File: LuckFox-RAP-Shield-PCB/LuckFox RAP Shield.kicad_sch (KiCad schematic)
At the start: 4 parts, among them J1 LuckFox_Pico_Mini_Connector, J2 External_5V_Input_from_Buck_M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, U2 W5500_Ethernet_Module_DNP_on_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

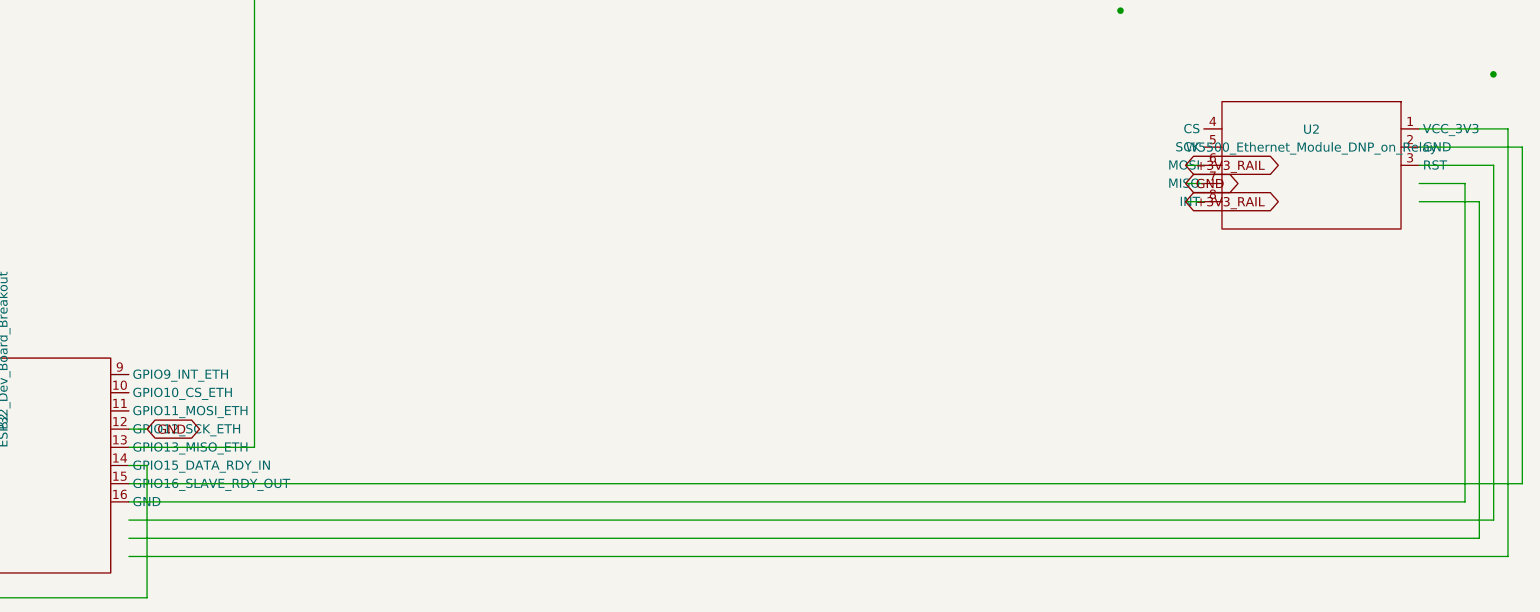
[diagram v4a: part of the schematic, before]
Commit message: Fix U2 wiring: account for its (mirror y) placement flag
U2's instance has a mirror-y flag (set from before this session) that
I missed when computing its pin positions -- both when generating the
SPI-ETH wires/power-rail labels and when validating them, so the
validation was checking its own wrong assumption and passed anyway.
Net effect: CS/SCK/MOSI/MISO/INT are actually on U2's west side and
VCC_3V3/GND/RST on the east, the opposite of what was wired, which is
exactly what was visible in KiCad as wires landing away from the pins.

Recomputed U2's true pin positions with the mirror transform applied
and rerouted the 5 SPI-ETH wires and 3 power-rail label stubs to
match. Re-verified with a corrected, mirror-aware version of the
netlist tracer (all 14 nets correct, zero stray/unconnected pins).
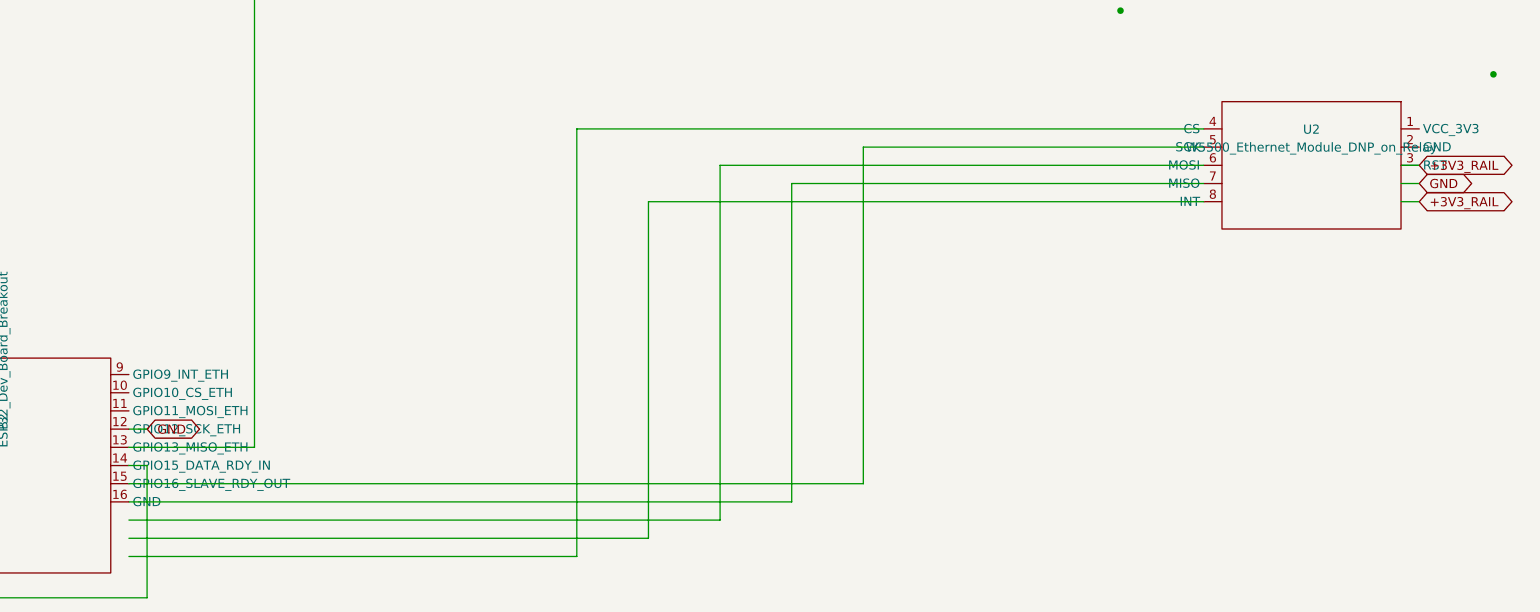
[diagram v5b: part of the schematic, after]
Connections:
- net +3V3_RAIL: now also U2.3 (RST)
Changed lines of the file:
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@@
 	(wire
 		(pts
-			(xy 77.47 189.23) (xy 270 189.23)
-		)
-		(stroke
-			(width 0)
-			(type default)
-		)
-	)
-	(wire
-		(pts
-			(xy 270 189.23) (xy 270 129.54)
-		)
-		(stroke
-			(width 0)
-			(type default)
-		)
-	)
-	(wire
-		(pts
-			(xy 270 129.54) (xy 257.61 129.54)
-		)
-		(stroke
-			(width 0)
-			(type default)
-		)
-	)
-	(wire
-		(pts
-			(xy 77.47 186.69) (xy 266 186.69)
-		)
-		(stroke
-			(width 0)
-			(type default)
-		)
-	)
-	(wire
-		(pts
-			(xy 266 186.69) (xy 266 139.7)
-		)
-		(stroke
-			(width 0)
-			(type default)
-		)
-	)
-	(wire
-		(pts
-			(xy 266 139.7) (xy 257.61 139.7)
-		)
-		(stroke
-			(width 0)
-			(type default)
-		)
-	)
-	(wire
-		(pts
-			(xy 77.47 184.15) (xy 268 184.15)
-		)
-		(stroke
-			(width 0)
-			(type default)
-		)
-	)
-	(wire
-		(pts
-			(xy 268 184.15) (xy 268 134.62)
-		)
-		(stroke
-			(width 0)
-			(type default)
-		)
-	)
-	(wire
-		(pts
-			(xy 268 134.62) (xy 257.61 134.62)
-		)
-		(stroke
-			(width 0)
-			(type default)
-		)
-	)
-	(wire
-		(pts
-			(xy 77.47 181.61) (xy 264 181.61)
-		)
-		(stroke
-			(width 0)
-			(type default)
-		)
-	)
-	(wire
-		(pts
-			(xy 264 181.61) (xy 264 137.16)
-		)
-		(stroke
-			(width 0)
-			(type default)
-		)
-	)
-	(wire
-		(pts
-			(xy 264 137.16) (xy 257.61 137.16)
-		)
-		(stroke
-			(width 0)
-			(type default)
-		)
-	)
-	(wire
-		(pts
-			(xy 77.47 179.07) (xy 272 179.07)
-		)
-		(stroke
-			(width 0)
-			(type default)
-		)
-	)
-	(wire
-		(pts
-			(xy 272 179.07) (xy 272 132.08)
-		)
-		(stroke
-			(width 0)
-			(type default)
-		)
-	)
-	(wire
-		(pts
-			(xy 272 132.08) (xy 257.61 132.08)
+			(xy 77.47 189.23) (xy 140 189.23)
+		)
+		(stroke
+			(width 0)
+			(type default)
+		)
+	)
+	(wire
+		(pts
+			(xy 140 189.23) (xy 140 129.54)
+		)
+		(stroke
+			(width 0)
+			(type default)
+		)
+	)
+	(wire
+		(pts
+			(xy 140 129.54) (xy 227.53 129.54)
+		)
+		(stroke
+			(width 0)
+			(type default)
+		)
+	)
+	(wire
+		(pts
+			(xy 77.47 186.69) (xy 150 186.69)
+		)
+		(stroke
+			(width 0)
+			(type default)
+		)
+	)
+	(wire
+		(pts
+			(xy 150 186.69) (xy 150 139.7)
+		)
+		(stroke
+			(width 0)
+			(type default)
+		)
+	)
+	(wire
+		(pts
+			(xy 150 139.7) (xy 227.53 139.7)
+		)
+		(stroke
+			(width 0)
+			(type default)
+		)
+	)
+	(wire
+		(pts
+			(xy 77.47 184.15) (xy 160 184.15)
+		)
+		(stroke
+			(width 0)
+			(type default)
+		)
+	)
+	(wire
+		(pts
+			(xy 160 184.15) (xy 160 134.62)
+		)
+		(stroke
+			(width 0)
+			(type default)
+		)
+	)
+	(wire
+		(pts
+			(xy 160 134.62) (xy 227.53 134.62)
+		)
+		(stroke
+			(width 0)
+			(type default)
+		)
+	)
+	(wire
+		(pts
+			(xy 77.47 181.61) (xy 170 181.61)
+		)
+		(stroke
+			(width 0)
+			(type default)
+		)
+	)
+	(wire
+		(pts
+			(xy 170 181.61) (xy 170 137.16)
+		)
+		(stroke
+			(width 0)
+			(type default)
+		)
+	)
+	(wire
+		(pts
+			(xy 170 137.16) (xy 227.53 137.16)
+		)
+		(stroke
+			(width 0)
+			(type default)
+		)
+	)
+	(wire
+		(pts
+			(xy 77.47 179.07) (xy 180 179.07)
+		)
+		(stroke
+			(width 0)
+			(type default)
+		)
+	)
+	(wire
+		(pts
+			(xy 180 179.07) (xy 180 132.08)
+		)
+		(stroke
+			(width 0)
+			(type default)
+		)
+	)
+	(wire
+		(pts
+			(xy 180 132.08) (xy 227.53 132.08)
 		)
 		(stroke
@@
 	(wire
 		(pts
-			(xy 227.53 137.16) (xy 224.99 137.16)
-		)
-		(stroke
-			(width 0)
-			(type default)
-		)
-	)
-	(global_label "GND"
-		(shape bidirectional)
-		(at 224.99 137.16 0)
-		(effects
-			(font
-				(size 1.27 1.27)
-			)
-			(justify left)
-		)
-		(property "Intersheetrefs" "${INTERSHEET_REFS}"
-			(at 224.99 137.16 0)
+			(xy 255.07 137.16) (xy 257.61 137.16)
+		)
+		(stroke
+			(width 0)
+			(type default)
+		)
+	)
+	(global_label "GND"
+		(shape bidirectional)
+		(at 257.61 137.16 0)
+		(effects
+			(font
+				(size 1.27 1.27)
+			)
+			(justify left)
+		)
+		(property "Intersheetrefs" "${INTERSHEET_REFS}"
+			(at 257.61 137.16 0)
+			(hide yes)
+			(show_name no)
+			(do_not_autoplace no)
+			(effects
+				(font
+					(size 1.27 1.27)
+				)
+			)
+		)
+	)
+	(wire
+		(pts
+			(xy 255.07 139.7) (xy 257.61 139.7)
+		)
+		(stroke
+			(width 0)
+			(type default)
+		)
+	)
+	(global_label "+3V3_RAIL"
+		(shape bidirectional)
+		(at 257.61 139.7 0)
+		(effects
+			(font
+				(size 1.27 1.27)
+			)
+			(justify left)
+		)
+		(property "Intersheetrefs" "${INTERSHEET_REFS}"
+			(at 257.61 139.7 0)
+			(hide yes)
+			(show_name no)
+			(do_not_autoplace no)
+			(effects
+				(font
+					(size 1.27 1.27)
+				)
+			)
+		)
+	)
+	(wire
+		(pts
+			(xy 255.07 134.62) (xy 257.61 134.62)
+		)
+		(stroke
+			(width 0)
+			(type default)
+		)
+	)
+	(global_label "+3V3_RAIL"
+		(shape bidirectional)
+		(at 257.61 134.62 0)
+		(effects
+			(font
+				(size 1.27 1.27)
+			)
+			(justify left)
+		)
+		(property "Intersheetrefs" "${INTERSHEET_REFS}"
+			(at 257.61 134.62 0)
 			(hide yes)
 			(show_name no)
@@
 			(hide yes)
 			(show_name no)
-			(do_not_autoplace no)
-			(effects
-				(font
-					(size 1.27 1.27)
-				)
-			)
-		)
-	)
-	(wire
-		(pts
-			(xy 227.53 139.7) (xy 224.99 139.7)
-		)
-		(stroke
-			(width 0)
-			(type default)
-		)
-	)
-	(global_label "+3V3_RAIL"
-		(shape bidirectional)
-		(at 224.99 139.7 0)
-		(effects
-			(font
-				(size 1.27 1.27)
-			)
-			(justify left)
-		)
-		(property "Intersheetrefs" "${INTERSHEET_REFS}"
-			(at 224.99 139.7 0)
-			(hide yes)
-			(show_name no)
-			(do_not_autoplace no)
-			(effects
-				(font
-					(size 1.27 1.27)
-				)
-			)
-		)
-	)
-	(wire
-		(pts
-			(xy 227.53 134.62) (xy 224.99 134.62)
-		)
-		(stroke
-			(width 0)
-			(type default)
-		)
-	)
-	(global_label "+3V3_RAIL"
-		(shape bidirectional)
-		(at 224.99 134.62 0)
-		(effects
-			(font
-				(size 1.27 1.27)
-			)
-			(justify left)
-		)
-		(property "Intersheetrefs" "${INTERSHEET_REFS}"
-			(at 224.99 134.62 0)
-			(hide yes)
-			(show_name no)

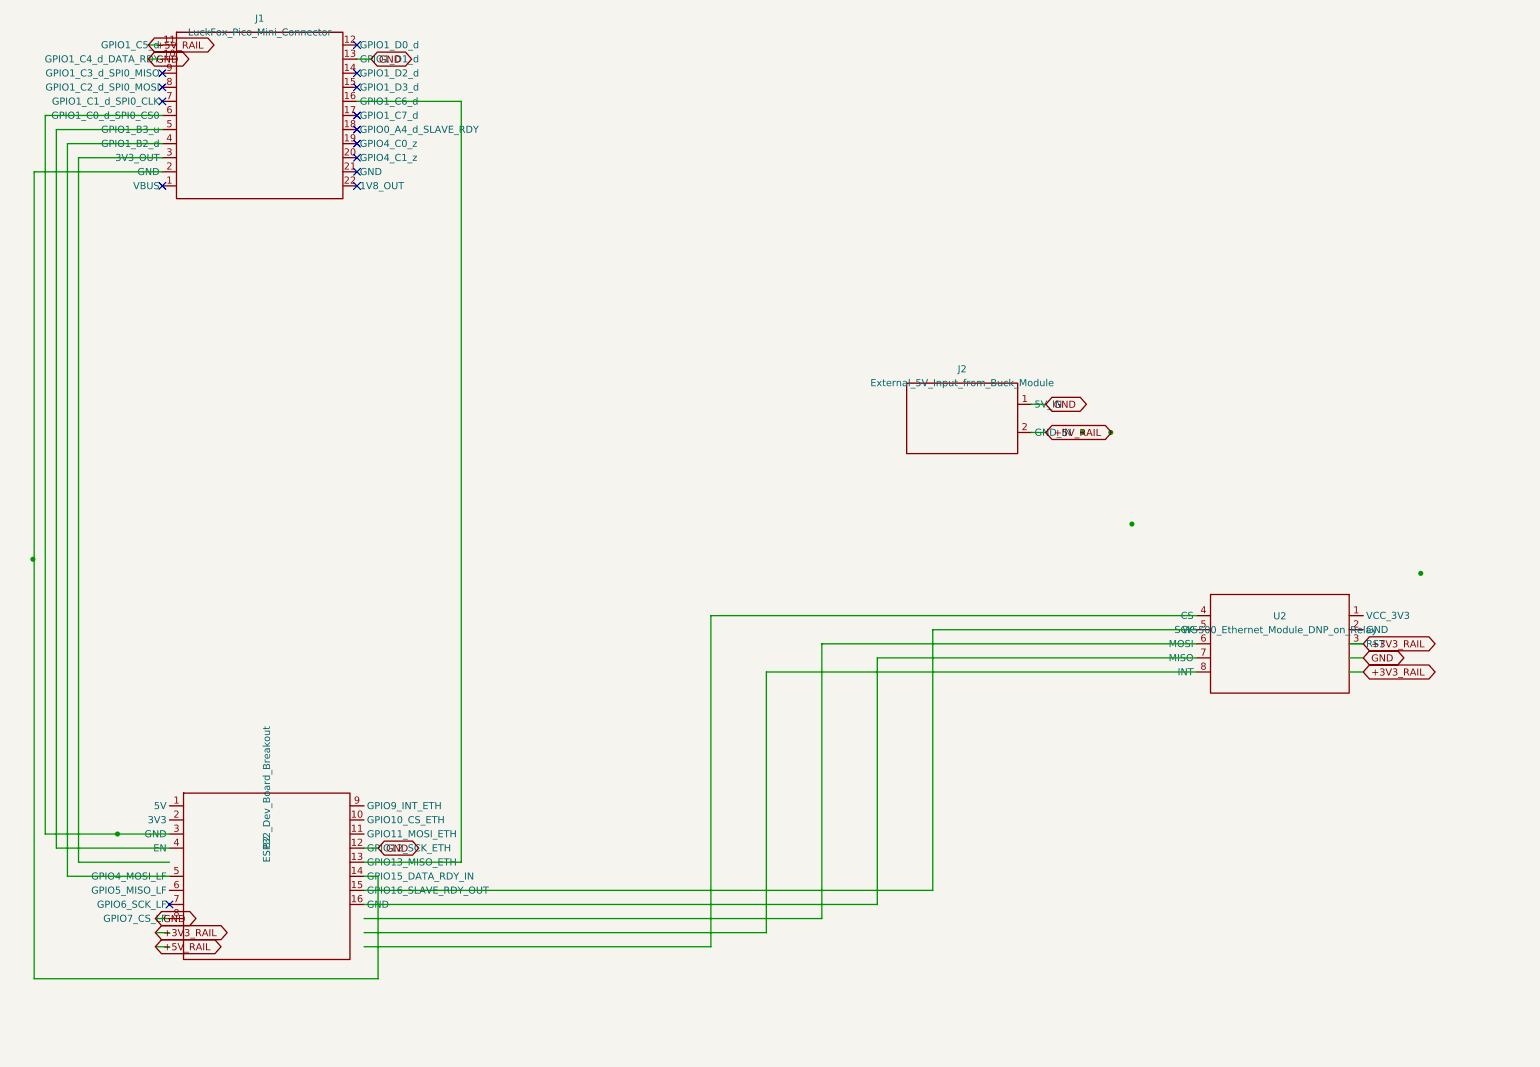
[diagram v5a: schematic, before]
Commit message: Lengthen global-label stubs and fix a masked U2 pin-position bug
Global label stubs were only 2.54mm (same as the pin length itself),
so label hexagons sat right on top of neighboring pins' name text --
visually indistinguishable from a real disconnection, which is what
was showing up in KiCad. Lengthened all 12 stubs to 15mm.

While doing this, found the U2 power-rail wires (VCC_3V3/GND/RST)
were anchored 2.54mm short of the true pin tip -- a manual arithmetic
slip in the earlier mirror fix (forgot to add the pin's own length
after mirroring) that happened to still connect only because the old
short stub's far end coincidentally landed exactly on the real pin.
Extending the stub from that wrong anchor would have broken it, so
corrected the anchor to the true pin position (257.61, not 255.07)
before extending.

Re-verified with the mirror-aware net tracer: all 14 nets correct,
zero unconnected/stray pins.
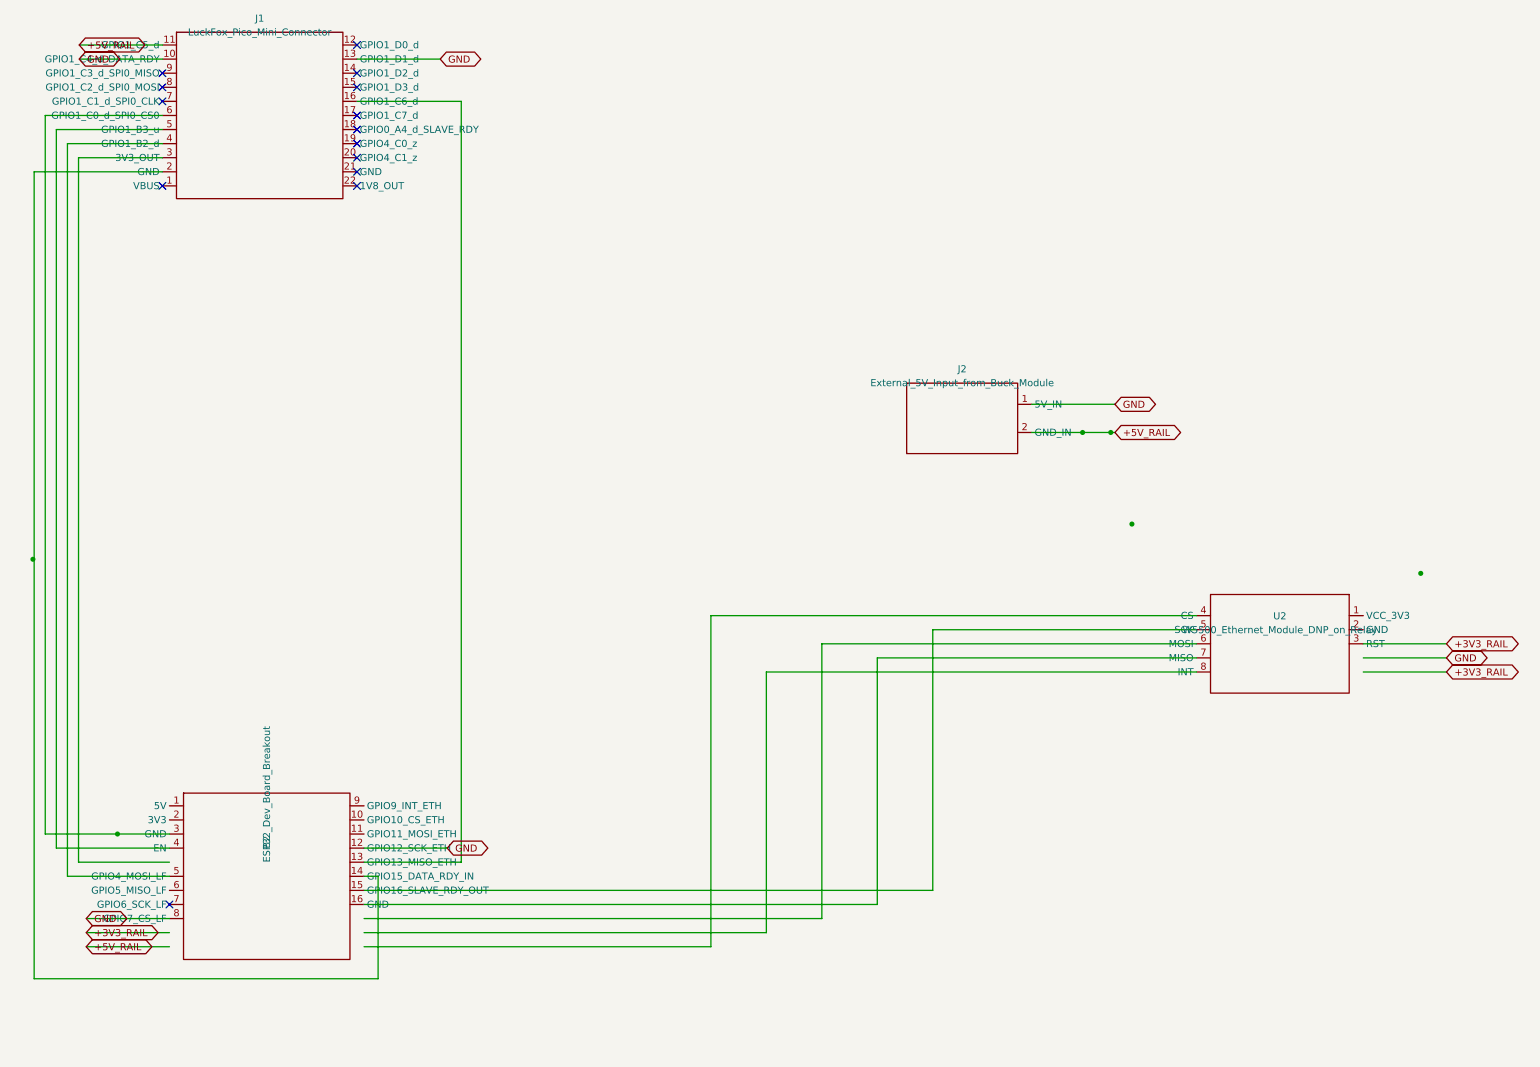
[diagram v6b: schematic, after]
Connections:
- net +3V3_RAIL: no longer U2.3 (RST)
